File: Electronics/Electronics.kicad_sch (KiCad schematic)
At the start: 51 parts, among them J3 Terminal1x2, J4 Terminal1x2, J5 Terminal1x2, J6 Terminal1x2, J7 Terminal1x2, K1 G3MB-202P, K2 G3MB-202P, K3 G3MB-202P, K4 G3MB-202P, U1 PC817, U2 PC817, U3 PC817, U4 PC817, U5 PC817, U6 PC817

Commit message: started 3D modelling enclosure
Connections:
- net at J4.1 (Pin_1): now also K2.1; no longer K2.2
- net at J4.2 (Pin_2): now also K2.2; no longer K2.1
- net at K3.1: now also J6.1 (Pin_1); no longer J6.2 (Pin_2)
- net at K3.2: now also J6.2 (Pin_2); no longer J6.1 (Pin_1)
- net at J7.1 (Pin_1): now also PS1.1 (AC/L); no longer PS1.2 (AC/N)
- net at J7.2 (Pin_2): now also PS1.2 (AC/N); no longer PS1.1 (AC/L)
- net at K4.1: now also J5.1 (Pin_1); no longer J5.2 (Pin_2)
- net at K4.2: now also J5.2 (Pin_2); no longer J5.1 (Pin_1)
- net at J3.1 (Pin_1): now also K1.1; no longer K1.2
- net at J3.2 (Pin_2): now also K1.2; no longer K1.1
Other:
- moved on the sheet: J3, J4, J5, J6, J7
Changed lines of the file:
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@@
 	(wire
 		(pts
-			(xy 218.44 31.75) (xy 218.44 35.56)
-		)
-		(stroke
-			(width 0)
-			(type default)
-		)
-	)
-	(wire
-		(pts
 			(xy 135.89 110.49) (xy 143.51 110.49)
 		)
@@
 	(wire
 		(pts
-			(xy 218.44 138.43) (xy 218.44 142.24)
+			(xy 199.39 48.26) (xy 199.39 50.8)
 		)
 		(stroke
@@
 	(wire
 		(pts
-			(xy 199.39 48.26) (xy 199.39 50.8)
+			(xy 111.76 110.49) (xy 120.65 110.49)
 		)
 		(stroke
@@
 	(wire
 		(pts
-			(xy 111.76 110.49) (xy 120.65 110.49)
+			(xy 218.44 48.26) (xy 218.44 50.8)
 		)
 		(stroke
@@
 	(wire
 		(pts
-			(xy 218.44 48.26) (xy 218.44 50.8)
+			(xy 204.47 55.88) (xy 209.55 55.88)
 		)
 		(stroke
@@
 	(wire
 		(pts
-			(xy 204.47 55.88) (xy 209.55 55.88)
+			(xy 199.39 162.56) (xy 204.47 162.56)
 		)
 		(stroke
@@
 	(wire
 		(pts
-			(xy 199.39 162.56) (xy 204.47 162.56)
+			(xy 210.82 162.56) (xy 218.44 162.56)
 		)
 		(stroke
@@
 	(wire
 		(pts
-			(xy 210.82 162.56) (xy 218.44 162.56)
+			(xy 218.44 67.31) (xy 218.44 71.12)
 		)
 		(stroke
@@
 	(wire
 		(pts
-			(xy 86.36 110.49) (xy 96.52 110.49)
+			(xy 218.44 102.87) (xy 218.44 106.68)
 		)
 		(stroke
@@
 	(wire
 		(pts
-			(xy 199.39 119.38) (xy 209.55 119.38)
+			(xy 86.36 110.49) (xy 96.52 110.49)
 		)
 		(stroke
@@
 	(wire
 		(pts
-			(xy 199.39 48.26) (xy 209.55 48.26)
+			(xy 199.39 119.38) (xy 209.55 119.38)
 		)
 		(stroke
@@
 	(wire
 		(pts
-			(xy 218.44 67.31) (xy 218.44 71.12)
+			(xy 199.39 48.26) (xy 209.55 48.26)
 		)
 		(stroke
@@
 	(wire
 		(pts
-			(xy 218.44 102.87) (xy 218.44 106.68)
+			(xy 218.44 138.43) (xy 218.44 142.24)
 		)
 		(stroke
@@
 	(wire
 		(pts
+			(xy 218.44 31.75) (xy 218.44 35.56)
+		)
+		(stroke
+			(width 0)
+			(type default)
+		)
+	)
+	(wire
+		(pts
 			(xy 218.44 132.08) (xy 218.44 135.89)
 		)
@@
 	(symbol
 		(lib_id "Connector:Screw_Terminal_01x02")
-		(at 213.36 67.31 180)
+		(at 213.36 64.77 0)
+		(mirror y)
 		(unit 1)
 		(exclude_from_sim no)
@@
 		(dnp no)
 		(property "Reference" "J4"
-			(at 208.026 66.548 90)
+			(at 208.026 65.532 90)
 			(effects
 				(font
@@
 		)
 		(property "Value" "Terminal1x2"
-			(at 210.058 66.294 90)
+			(at 210.058 65.786 90)
 			(effects
 				(font
@@
 		)
 		(property "Footprint" "TerminalBlock:TerminalBlock_bornier-2_P5.08mm"
-			(at 213.36 67.31 0)
+			(at 213.36 64.77 0)
 			(effects
 				(font
@@
 		)
 		(property "Datasheet" "~"
-			(at 213.36 67.31 0)
+			(at 213.36 64.77 0)
 			(effects
 				(font
@@
 		)
 		(property "Description" "Generic screw terminal, single row, 01x02, script generated (kicad-library-utils/schlib/autogen/connector/)"
-			(at 213.36 67.31 0)
+			(at 213.36 64.77 0)
 			(effects
 				(font
@@
 	(symbol
 		(lib_id "Connector:Screw_Terminal_01x02")
-		(at 41.91 52.07 180)
+		(at 41.91 49.53 0)
+		(mirror y)
 		(unit 1)
 		(exclude_from_sim no)
@@
 		(dnp no)
 		(property "Reference" "J7"
-			(at 36.576 51.308 90)
+			(at 36.576 50.292 90)
 			(effects
 				(font
@@
 		)
 		(property "Value" "Terminal1x2"
-			(at 38.608 51.054 90)
+			(at 38.608 50.546 90)
 			(effects
 				(font
@@
 		)
 		(property "Footprint" "TerminalBlock:TerminalBlock_bornier-2_P5.08mm"
-			(at 41.91 52.07 0)
+			(at 41.91 49.53 0)
 			(effects
 				(font
@@
 		)
 		(property "Datasheet" "~"
-			(at 41.91 52.07 0)
+			(at 41.91 49.53 0)
 			(effects
 				(font
@@
 		)
 		(property "Description" "Generic screw terminal, single row, 01x02, script generated (kicad-library-utils/schlib/autogen/connector/)"
-			(at 41.91 52.07 0)
+			(at 41.91 49.53 0)
 			(effects
 				(font
@@
 	(symbol
 		(lib_id "Connector:Screw_Terminal_01x02")
-		(at 213.36 138.43 180)
+		(at 213.36 135.89 0)
+		(mirror y)
 		(unit 1)
 		(exclude_from_sim no)
@@
 		(dnp no)
 		(property "Reference" "J6"
-			(at 208.026 137.668 90)
+			(at 208.026 136.652 90)
 			(effects
 				(font
@@
 		)
 		(property "Value" "Terminal1x2"
-			(at 210.058 137.414 90)
+			(at 210.058 136.906 90)
 			(effects
 				(font
@@
 		)
 		(property "Footprint" "TerminalBlock:TerminalBlock_bornier-2_P5.08mm"
-			(at 213.36 138.43 0)
+			(at 213.36 135.89 0)
 			(effects
 				(font
@@
 		)
 		(property "Datasheet" "~"
-			(at 213.36 138.43 0)
+			(at 213.36 135.89 0)
 			(effects
 				(font
@@
 		)
 		(property "Description" "Generic screw terminal, single row, 01x02, script generated (kicad-library-utils/schlib/autogen/connector/)"
-			(at 213.36 138.43 0)
+			(at 213.36 135.89 0)
 			(effects
 				(font
@@
 	(symbol
 		(lib_id "Connector:Screw_Terminal_01x02")
-		(at 213.36 31.75 180)
+		(at 213.36 29.21 0)
+		(mirror y)
 		(unit 1)
 		(exclude_from_sim no)
@@
 		(dnp no)
 		(property "Reference" "J3"
-			(at 208.026 30.988 90)
+			(at 208.026 29.972 90)
 			(effects
 				(font
@@
 		)
 		(property "Value" "Terminal1x2"
-			(at 210.058 30.734 90)
+			(at 210.058 30.226 90)
 			(effects
 				(font
@@
 		)
 		(property "Footprint" "TerminalBlock:TerminalBlock_bornier-2_P5.08mm"
-			(at 213.36 31.75 0)
+			(at 213.36 29.21 0)
 			(effects
 				(font
@@
 		)
 		(property "Datasheet" "~"
-			(at 213.36 31.75 0)
+			(at 213.36 29.21 0)
 			(effects
 				(font
@@
 		)
 		(property "Description" "Generic screw terminal, single row, 01x02, script generated (kicad-library-utils/schlib/autogen/connector/)"
-			(at 213.36 31.75 0)
+			(at 213.36 29.21 0)
 			(effects
 				(font
@@
 	(symbol
 		(lib_id "Connector:Screw_Terminal_01x02")
-		(at 213.36 102.87 180)
+		(at 213.36 100.33 0)
+		(mirror y)
 		(unit 1)
 		(exclude_from_sim no)
@@
 		(dnp no)
 		(property "Reference" "J5"
-			(at 208.026 102.108 90)
+			(at 208.026 101.092 90)
 			(effects
 				(font
@@
 		)
 		(property "Value" "Terminal1x2"
-			(at 210.058 101.854 90)
+			(at 210.058 101.346 90)
 			(effects
 				(font
@@
 		)
 		(property "Footprint" "TerminalBlock:TerminalBlock_bornier-2_P5.08mm"
-			(at 213.36 102.87 0)
+			(at 213.36 100.33 0)
 			(effects
 				(font
@@
 		)
 		(property "Datasheet" "~"
-			(at 213.36 102.87 0)
+			(at 213.36 100.33 0)
 			(effects
 				(font
@@
 		)
 		(property "Description" "Generic screw terminal, single row, 01x02, script generated (kicad-library-utils/schlib/autogen/connector/)"
-			(at 213.36 102.87 0)
+			(at 213.36 100.33 0)
 			(effects
 				(font

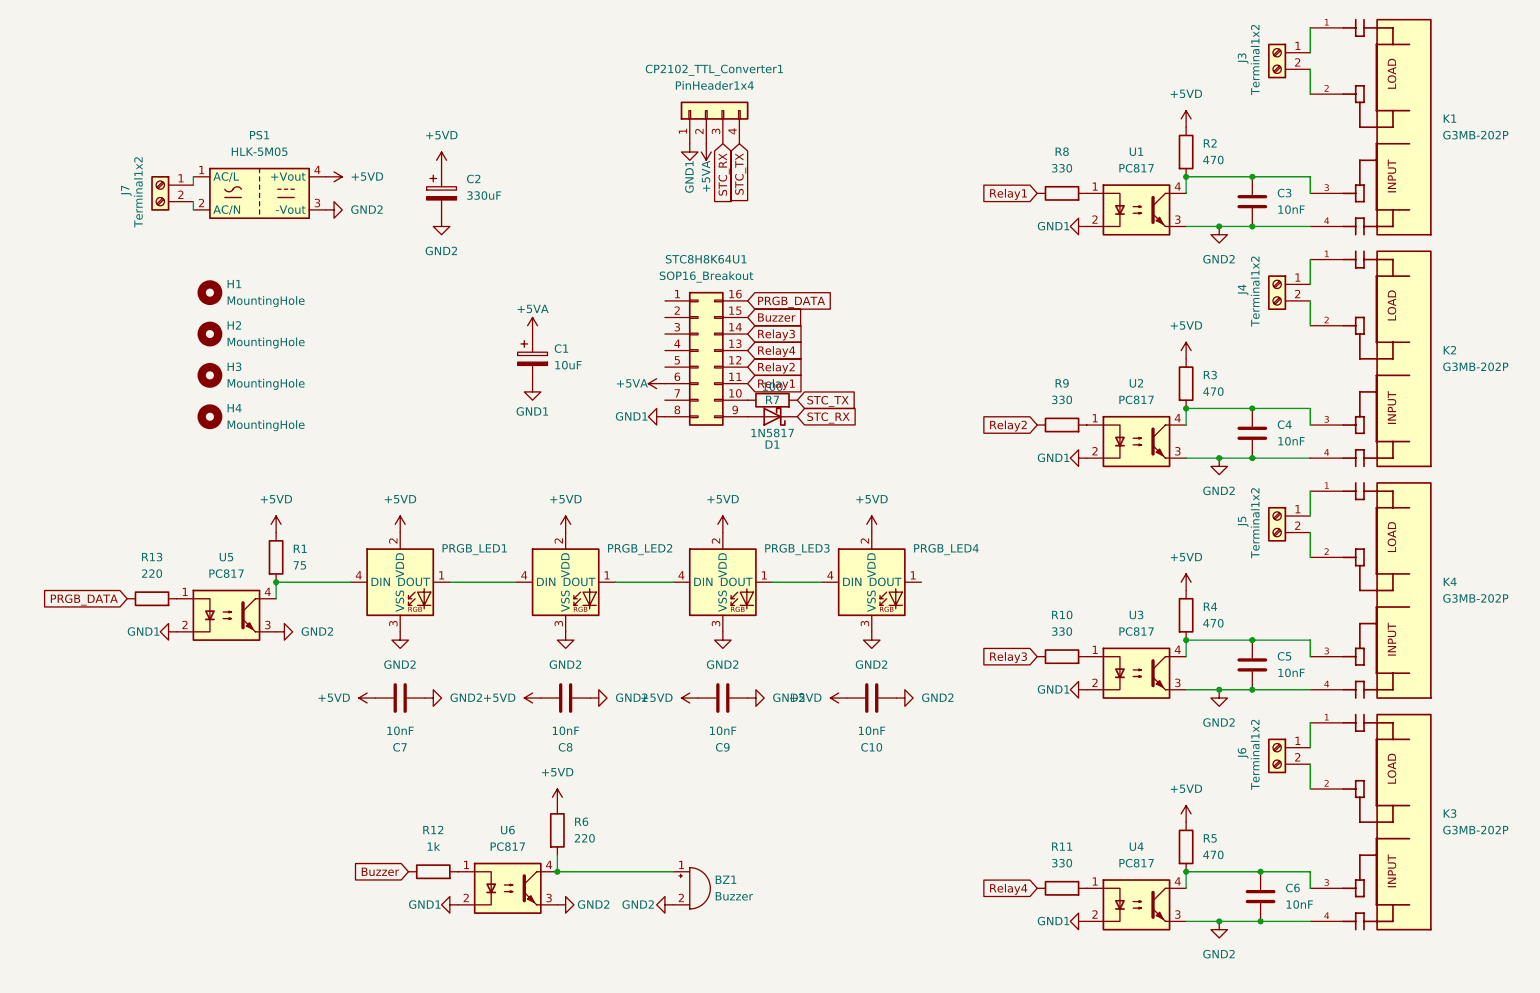
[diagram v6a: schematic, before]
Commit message: added schematic and PCB layout for mechanical relays
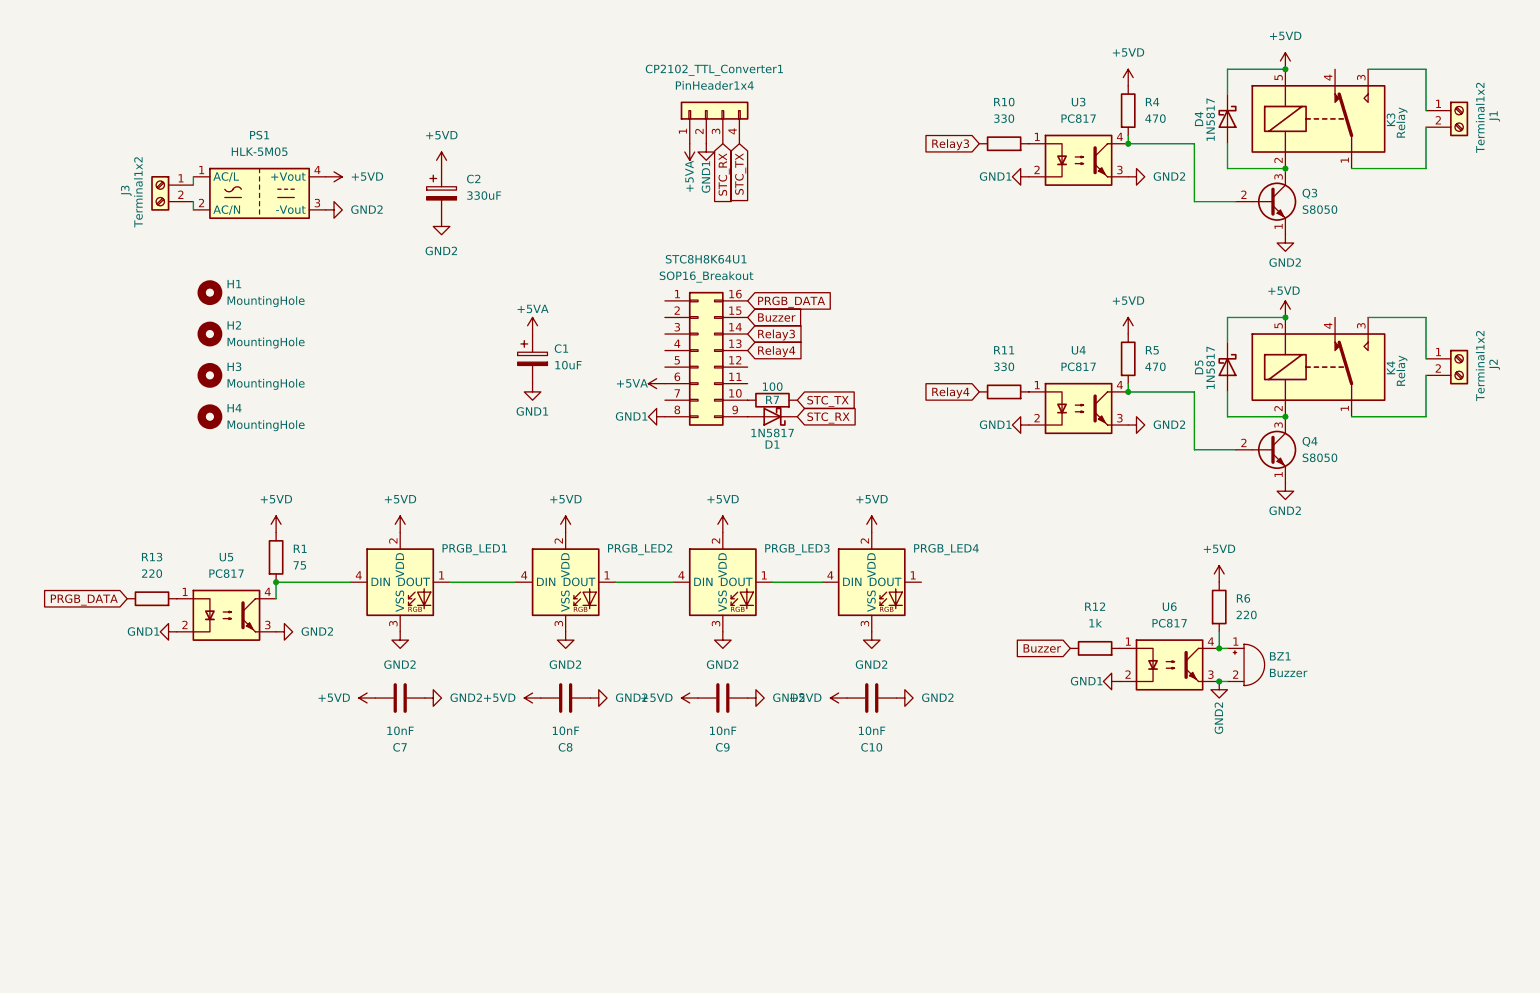
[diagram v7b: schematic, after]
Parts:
- removed C3, C4, C5, C6: 10nF, Capacitor_THT:C_Disc_D5.0mm_W2.5mm_P2.50mm, symbol Device:C
- removed J4, J5, J6, J7: Terminal1x2, TerminalBlock:TerminalBlock_bornier-2_P5.08mm, symbol Connector:Screw_Terminal_01x02
- removed K1, K2, K3, K4: G3MB-202P, G3MB-202P:RELAY_G3MB-202P, symbol G3MB-202P:G3MB-202P
- removed R2, R3: 470, Resistor_THT:R_Axial_DIN0207_L6.3mm_D2.5mm_P7.62mm_Horizontal, symbol Device:R
- removed R8, R9: 330, Resistor_THT:R_Axial_DIN0207_L6.3mm_D2.5mm_P7.62mm_Horizontal, symbol Device:R
- removed U1, U2: PC817, Package_DIP:DIP-4_W7.62mm, symbol Isolator:PC817
- added D4, D5: 1N5817, Diode_THT:D_DO-41_SOD81_P7.62mm_Horizontal, symbol Diode:1N5817
- added J1, J2: Terminal1x2, TerminalBlock:TerminalBlock_bornier-2_P5.08mm, symbol Connector:Screw_Terminal_01x02
- added K3, K4: Relay, Relay_THT:Relay_SPDT_SANYOU_SRD_Series_Form_C, symbol Relay:SANYOU_SRD_Form_C
- added Q3, Q4: S8050, Package_TO_SOT_THT:TO-92_Inline_Wide, symbol Transistor_BJT:S8050
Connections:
- net +5VA: now also CP2102_TTL_Converter1.1 (Pin_1); no longer CP2102_TTL_Converter1.2 (Pin_2)
- net +5VD: now also D4.1 (K), D5.1 (K), K3.5, K4.5
- net GND1: now also CP2102_TTL_Converter1.2 (Pin_2); no longer CP2102_TTL_Converter1.1 (Pin_1)
- net GND2: now also Q3.1 (E), Q4.1 (E)
- net at R4.2, U3.4: now also Q3.2 (B)
- net at R5.2, U4.4: now also Q4.2 (B)
- net at PS1.1 (AC/L): now also J3.1 (Pin_1)
- net at PS1.2 (AC/N): now also J3.2 (Pin_2)
- net Relay1: no longer names the net of STC8H8K64U1.11 (Pin_11)
- net Relay2: no longer names the net of STC8H8K64U1.12 (Pin_12)
- new net: D4.2 (A), K3.2, Q3.3 (C)
- new net: J1.1 (Pin_1), K3.3
- new net: J1.2 (Pin_2), K3.1
- new net: D5.2 (A), K4.2, Q4.3 (C)
- new net: J2.2 (Pin_2), K4.1
- new net: J2.1 (Pin_1), K4.3
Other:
- moved on the sheet: BZ1, R10, R11, R12, R4, R5, R6, U3, U4, U6

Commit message: added temperature sensor and AC detect schematic and PCB layout
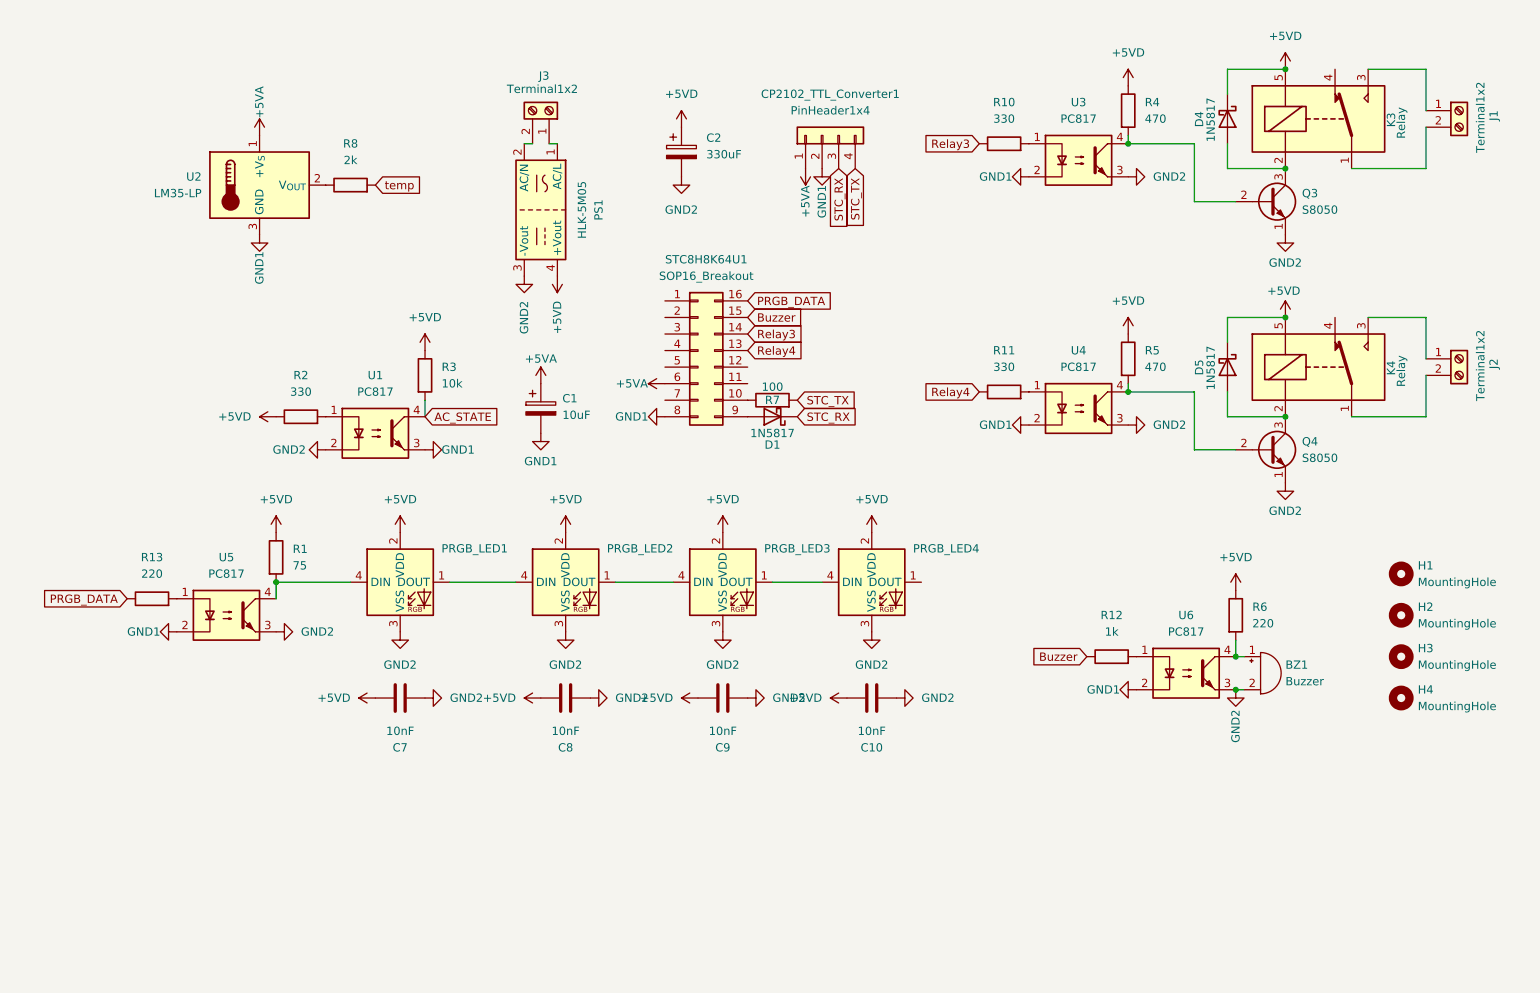
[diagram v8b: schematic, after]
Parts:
- added R2: 330, Resistor_THT:R_Axial_DIN0207_L6.3mm_D2.5mm_P7.62mm_Horizontal, symbol Device:R
- added R3: 10k, Resistor_THT:R_Axial_DIN0207_L6.3mm_D2.5mm_P7.62mm_Horizontal, symbol Device:R
- added R8: 2k, Resistor_THT:R_Axial_DIN0207_L6.3mm_D2.5mm_P7.62mm_Horizontal, symbol Device:R
- added U1: PC817, Package_DIP:DIP-4_W7.62mm, symbol Isolator:PC817
- added U2: LM35-LP, Package_TO_SOT_THT:TO-92L_Inline_Wide, symbol Sensor_Temperature:LM35-LP
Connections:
- net +5VA: now also U2.1 (+V_{S})
- net +5VD: now also R2.1, R3.1
- net GND1: now also U1.3, U2.3 (GND)
- net GND2: now also U1.2
- new net: R8.1, U2.2 (V_{OUT})
- new net: R2.2, U1.1
- new net AC_STATE: R3.2, U1.4
- new net temp: R8.2
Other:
- moved on the sheet: BZ1, C1, C2, CP2102_TTL_Converter1, H1, H2, H3, H4, J3, PS1, R12, R6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
